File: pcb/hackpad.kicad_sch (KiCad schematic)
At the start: 32 parts, among them SW1 SW_Push, SW2 SW_Push, SW3 RotaryEncoder_Switch, SW4 SW_Push, SW5 SW_Push, SW6 SW_Push, SW7 SW_Push, SW8 SW_Push, SW9 SW_Push, U1 XIAO-RP2040-DIP

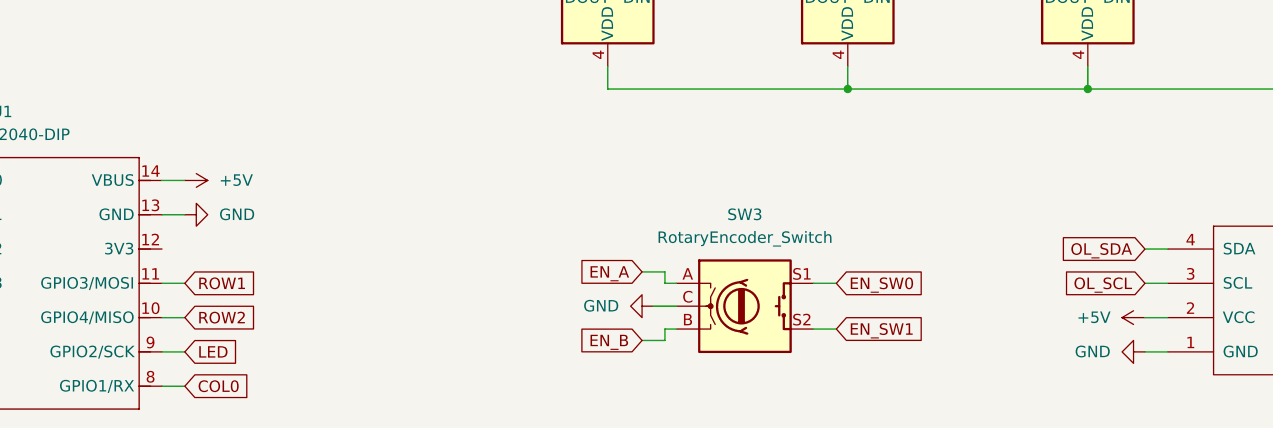
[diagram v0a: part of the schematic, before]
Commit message: Fix OLED voltage
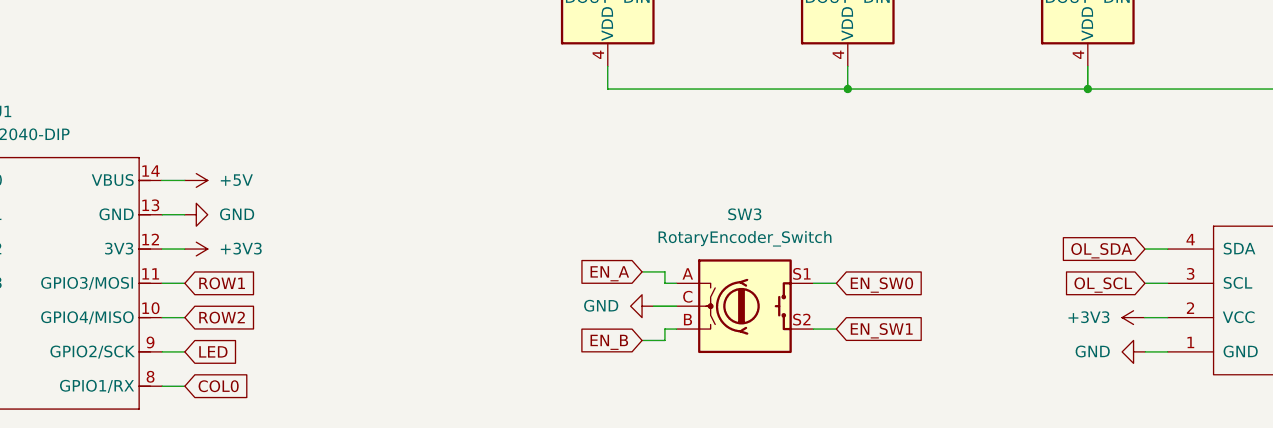
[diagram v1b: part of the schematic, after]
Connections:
- net +5V: no longer OL1.2 (VCC)
- net +3V3: now reaches U1.12 (3V3)
- net +3V3: now also OL1.2 (VCC)
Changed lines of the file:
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@@
 	(wire
 		(pts
+			(xy 100.33 128.27) (xy 102.87 128.27)
+		)
+		(stroke
+			(width 0)
+			(type default)
+		)
+	)
+	(wire
+		(pts
 			(xy 149.86 49.53) (xy 149.86 52.07)
 		)
@@
 	)
 	(symbol
+		(lib_id "power:+3V3")
+		(at 209.55 135.89 90)
+		(unit 1)
+		(exclude_from_sim no)
+		(in_bom yes)
+		(on_board yes)
+		(dnp no)
+		(fields_autoplaced yes)
+		(property "Reference" "#PWR04"
+			(at 213.36 135.89 0)
+			(effects
+				(font
+					(size 1.27 1.27)
+				)
+				(hide yes)
+			)
+		)
+		(property "Value" "+3V3"
+			(at 205.74 135.8899 90)
+			(effects
+				(font
+					(size 1.27 1.27)
+				)
+				(justify left)
+			)
+		)
+		(property "Footprint" ""
+			(at 209.55 135.89 0)
+			(effects
+				(font
+					(size 1.27 1.27)
+				)
+				(hide yes)
+			)
+		)
+		(property "Datasheet" ""
+			(at 209.55 135.89 0)
+			(effects
+				(font
+					(size 1.27 1.27)
+				)
+				(hide yes)
+			)
+		)
+		(property "Description" "Power symbol creates a global label with name \"+3V3\""
+			(at 209.55 135.89 0)
+			(effects
+				(font
+					(size 1.27 1.27)
+				)
+				(hide yes)
+			)
+		)
+		(pin "1"
+		)
+		(instances
+			(project "hackpad"
+				(path "/5ff51838-261f-4aee-b6fa-0b1893749192"
+					(reference "#PWR04")
+					(unit 1)
+				)
+			)
+		)
+	)
+	(symbol
 		(lib_id "Diode:1N4148")
 		(at 57.15 72.39 0)
@@
 	)
 	(symbol
-		(lib_id "power:+5V")
-		(at 209.55 135.89 90)
-		(unit 1)
-		(exclude_from_sim no)
-		(in_bom yes)
-		(on_board yes)
-		(dnp no)
-		(property "Reference" "#PWR04"
-			(at 213.36 135.89 0)
-			(effects
-				(font
-					(size 1.27 1.27)
-				)
-				(hide yes)
-			)
-		)
-		(property "Value" "+5V"
-			(at 205.74 135.8901 90)
-			(effects
-				(font
-					(size 1.27 1.27)
-				)
-				(justify left)
-			)
-		)
-		(property "Footprint" ""
-			(at 209.55 135.89 0)
-			(effects
-				(font
-					(size 1.27 1.27)
-				)
-				(hide yes)
-			)
-		)
-		(property "Datasheet" ""
-			(at 209.55 135.89 0)
-			(effects
-				(font
-					(size 1.27 1.27)
-				)
-				(hide yes)
-			)
-		)
-		(property "Description" "Power symbol creates a global label with name \"+5V\""
-			(at 209.55 135.89 0)
-			(effects
-				(font
-					(size 1.27 1.27)
-				)
-				(hide yes)
-			)
-		)
-		(pin "1"
-		)
-		(instances
-			(project "hackpad"
-				(path "/5ff51838-261f-4aee-b6fa-0b1893749192"
-					(reference "#PWR04")
-					(unit 1)
-				)
-			)
-		)
-	)
-	(symbol
 		(lib_id "Seeed_Studio_XIAO_Series:XIAO-RP2040-DIP")
 		(at 68.58 115.57 0)
@@
 					(unit 1)
 				)
+			)
+		)
+	)
+	(symbol
+		(lib_id "power:+3V3")
+		(at 102.87 128.27 270)
+		(unit 1)
+		(exclude_from_sim no)
+		(in_bom yes)
+		(on_board yes)
+		(dnp no)
+		(fields_autoplaced yes)
+		(property "Reference" "#PWR011"
+			(at 99.06 128.27 0)
+			(effects
+				(font
+					(size 1.27 1.27)
+				)
+				(hide yes)
+			)
+		)
+		(property "Value" "+3V3"
+			(at 106.68 128.2699 90)
+			(effects
+				(font
+					(size 1.27 1.27)
+				)
+				(justify left)
+			)
+		)
+		(property "Footprint" ""
+			(at 102.87 128.27 0)
+			(effects
+				(font
+					(size 1.27 1.27)
+				)
+				(hide yes)
+			)
+		)
+		(property "Datasheet" ""
+			(at 102.87 128.27 0)
+			(effects
+				(font
+					(size 1.27 1.27)
+				)
+				(hide yes)
+			)
+		)
+		(property "Description" "Power symbol creates a global label with name \"+3V3\""
+			(at 102.87 128.27 0)
+			(effects
+				(font
+					(size 1.27 1.27)
+				)
+				(hide yes)
+			)
+		)
+		(pin "1"
+		)
+		(instances
+			(project "hackpad"
+				(path "/5ff51838-261f-4aee-b6fa-0b1893749192"
+					(reference "#PWR011")
+					(unit 1)
+				)

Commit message: Update hackpad
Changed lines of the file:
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@@
 (kicad_sch
-	(version 20231120)
+	(version 20250114)
 	(generator "eeschema")
-	(generator_version "8.0")
+	(generator_version "9.0")
 	(paper "A4")
 	(junction
@@
 		)
 	)
+	(embedded_fonts no)
 )
